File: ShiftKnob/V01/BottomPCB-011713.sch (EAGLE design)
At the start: 20 parts, among them Q1 16MHz, U1 ATMEGA328, U2 MIC5205-5.0BM5

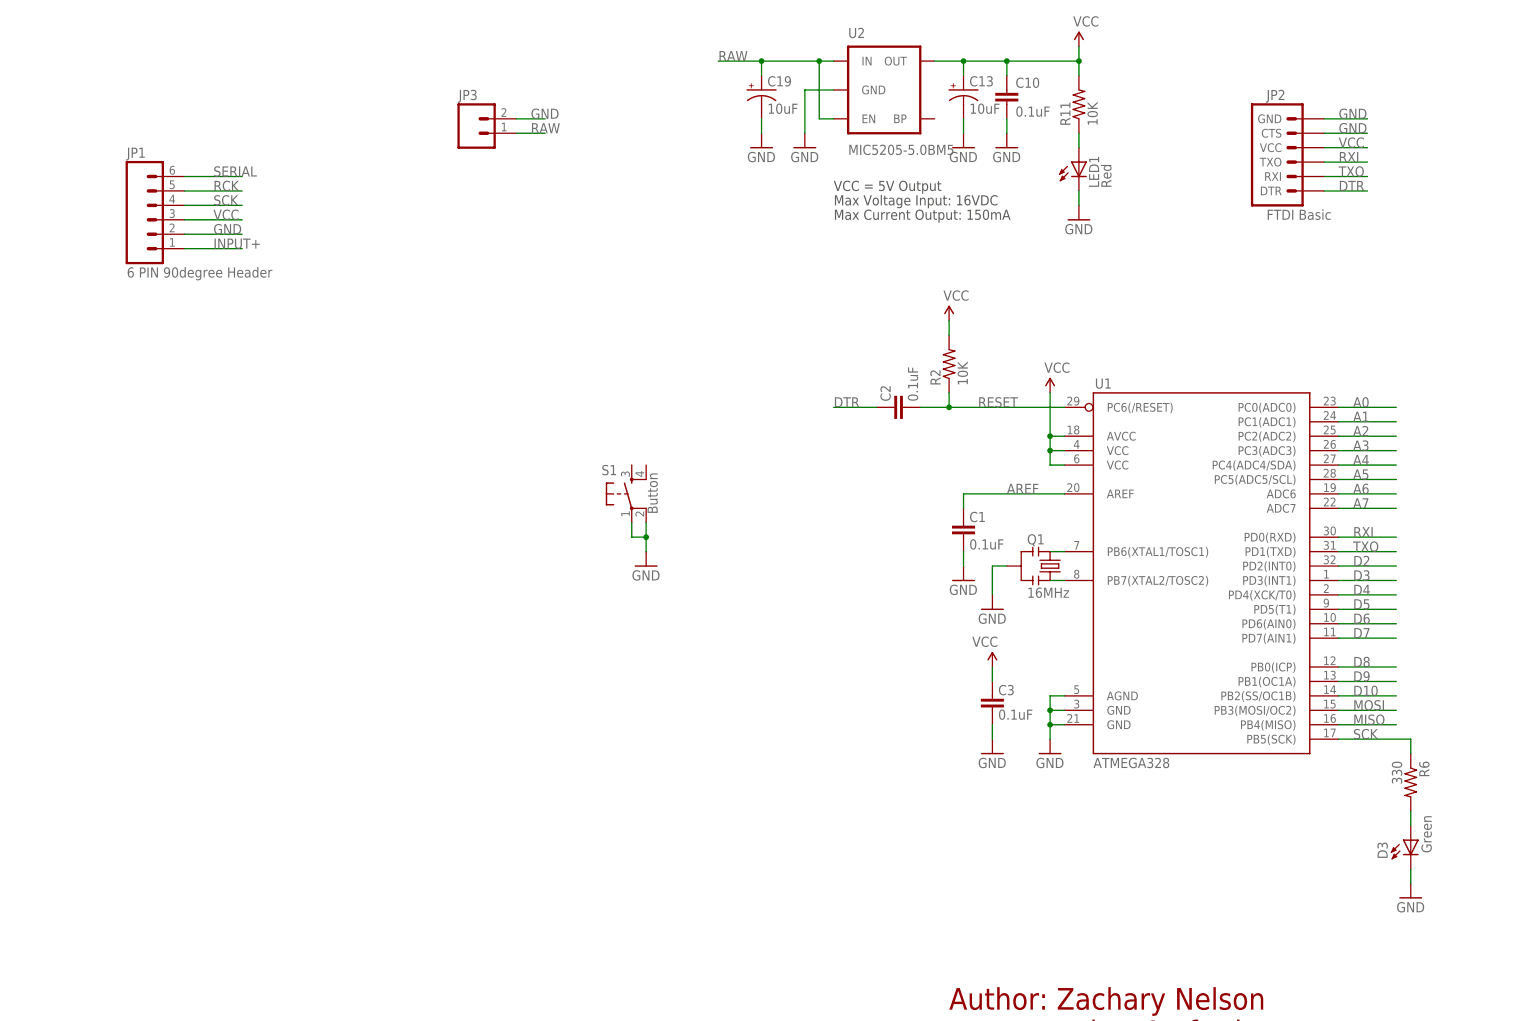
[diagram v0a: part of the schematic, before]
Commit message: all components added to BottomPCB schematic. added: MOSFETs, RGB LEDs x2, Motor connector, 7805 regulator
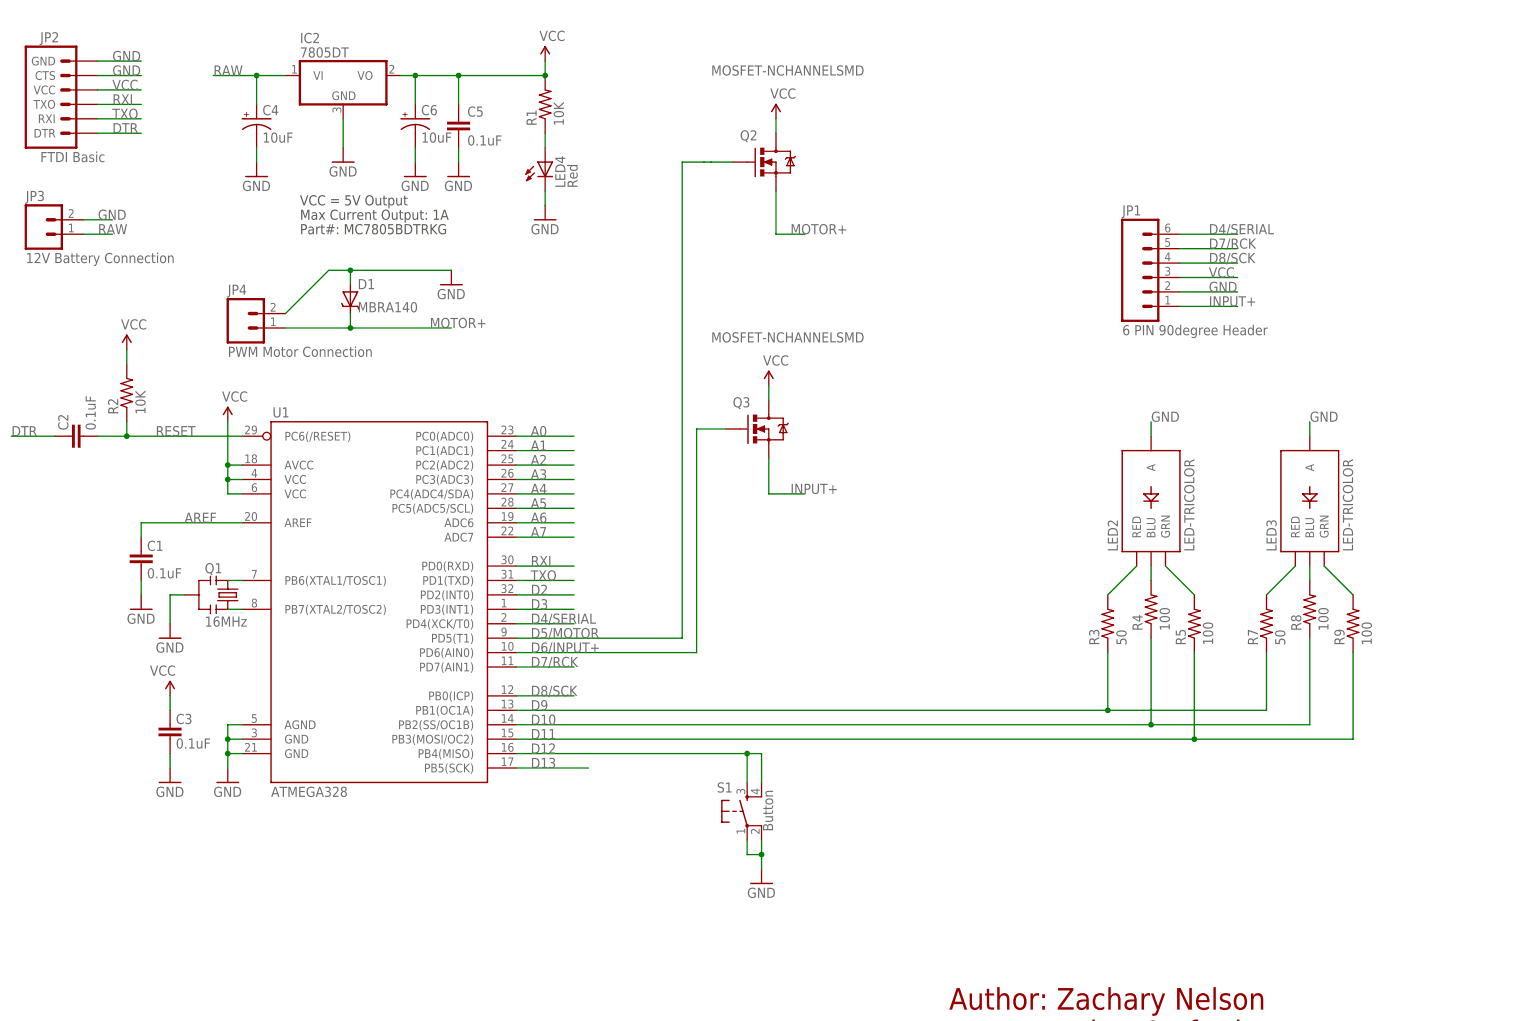
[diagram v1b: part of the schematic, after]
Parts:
- removed C10: 0.1uF, SparkFun:CAP0402-CAP
- removed C13, C19: 10uF, SparkFun:CAP_POL1206
- removed D3: Green, SparkFun:LED0603
- removed LED1: Red, SparkFun:LED0603
- removed R11: 10K, SparkFun:RESISTOR0402-RES
- removed R6: 330, SparkFun:RESISTOR0402-RES
- removed U2: MIC5205-5.0BM5, SparkFun:V_REG_LDOSMD
- added C4, C6: 10uF, SparkFun:CAP_POL1206
- added C5: 0.1uF, SparkFun:CAP0402-CAP
- added D1: MBRA140, SparkFun-DiscreteSemi:MBRA140
- added IC2: 7805DT, linear:7805DT
- added JP4: PWM Motor Connection, SparkFun-Connectors:M02POLAR
- added LED2, LED3: LED-TRICOLOR, SparkFun:LED-TRICOLOR
- added LED4: Red, SparkFun:LED0603
- added Q2, Q3: MOSFET-NCHANNELSMD, SparkFun-DiscreteSemi:MOSFET-NCHANNELSMD
- added R1: 10K, SparkFun:RESISTOR0402-RES
- added R3, R7: 50, SparkFun-Resistors:RESISTOR0805-RES
- added R4, R5, R8, R9: 100, SparkFun-Resistors:RESISTOR0805-RES
- JP3: value (none) -> 12V Battery Connection
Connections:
- removed net D4: U1.PD4(XCK/T0)
- removed net D5: U1.PD5(T1)
- removed net D6: U1.PD6(AIN0)
- removed net D7: U1.PD7(AIN1)
- removed net D8: U1.PB0(ICP)
- removed net MISO: U1.PB4(MISO)
- removed net MOSI: U1.PB3(MOSI/OC2)
- removed net N$38: LED1.A, R11.1
- removed net N$7: D3.A, R6.2
- removed net RCK: JP1.5
- removed net SCK: JP1.4, R6.1, U1.PB5(SCK)
- removed net SERIAL: JP1.6
- new net 3.3V: Q2.D, Q3.D
- new net D11: R5.1, R9.1, U1.PB3(MOSI/OC2)
- new net D12: S1.3, S1.4, U1.PB4(MISO)
- new net D13: U1.PB5(SCK)
- new net D4/SERIAL: JP1.6, U1.PD4(XCK/T0)
- new net D5/MOTOR: Q2.G, U1.PD5(T1)
- new net D6/INPUT+: Q3.G, U1.PD6(AIN0)
- new net D7/RCK: JP1.5, U1.PD7(AIN1)
- new net D8/SCK: JP1.4, U1.PB0(ICP)
- new net MOTOR+: D1.C, JP4.1, Q2.S
- new net N$16: LED3.BLU, R8.2
- new net N$25: LED2.BLU, R4.2
- new net N$3: LED4.A, R1.1
- new net N$4: LED2.RED, R3.2
- new net N$5: LED2.GRN, R5.2
- new net N$6: LED3.RED, R7.2
- new net N$8: LED3.GRN, R9.2
- net D10: now also R4.1, R8.1
- net D9: now also R3.1, R7.1
- net GND: now also C4.-, C5.2, C6.-, D1.A, IC2.GND, JP4.2, LED2.A, LED3.A, LED4.C; no longer C10.2, C13.-, C19.-, D3.C, LED1.C, U2.GND
- net INPUT+: now also Q3.S
- net RAW: now also C4.+, IC2.VI; no longer C19.+, U2.EN, U2.IN
- net VCC: now also C5.1, C6.+, IC2.VO, R1.2; no longer C10.1, C13.+, R11.2, U2.OUT
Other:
- note added: "Max Current Output: 1A"
- note added: "Part#: MC7805BDTRKG"
- note removed: "Max Current Output: 150mA"
- note removed: "Max Voltage Input: 16VDC"
- moved on the sheet: C1, C2, C3, JP1, JP2, JP3, Q1, R2, S1, U1

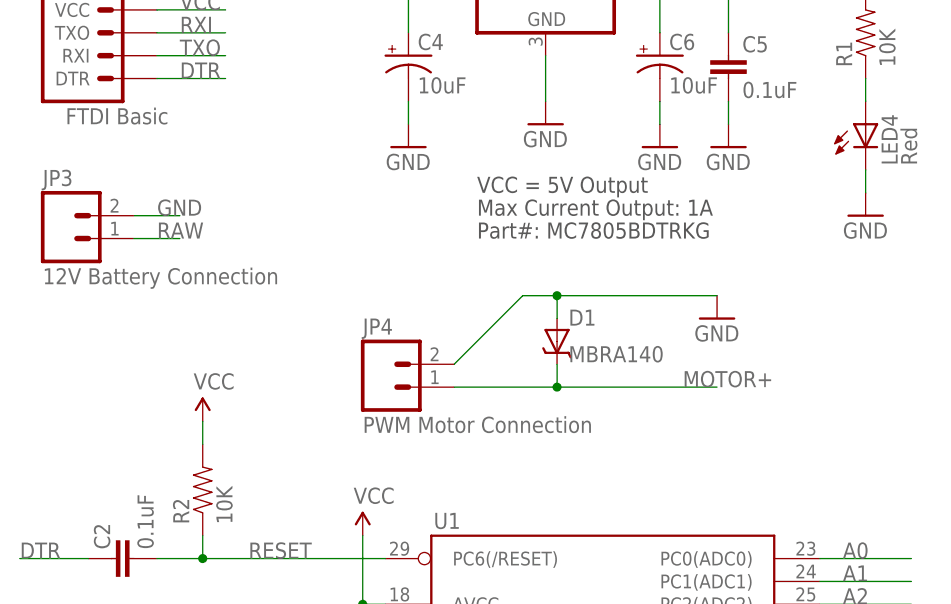
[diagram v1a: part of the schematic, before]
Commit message: change battery and motor connectors to SMT parts
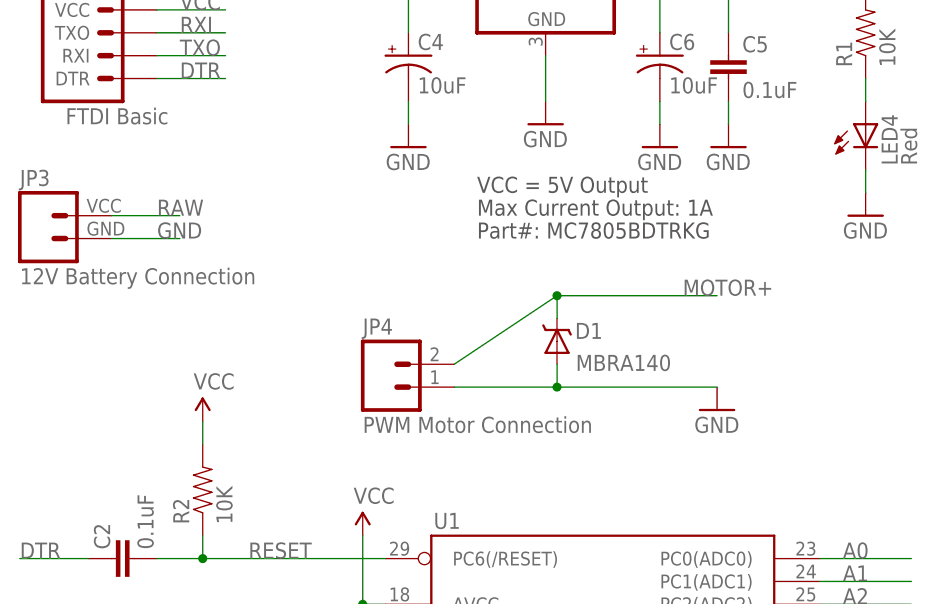
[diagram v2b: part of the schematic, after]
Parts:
- JP3: device SparkFun-Connectors:M02POLAR -> SparkFun-Connectors:M024UCON-15767
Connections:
- removed net 3.3V: Q2.D, Q3.D
- net GND: now also JP3.1, JP4.1; no longer JP3.2, JP4.2
- net MOTOR+: now also JP4.2; no longer JP4.1
- net RAW: now also JP3.2; no longer JP3.1
- net VCC: now also Q2.D, Q3.D
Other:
- moved on the sheet: D1, JP3

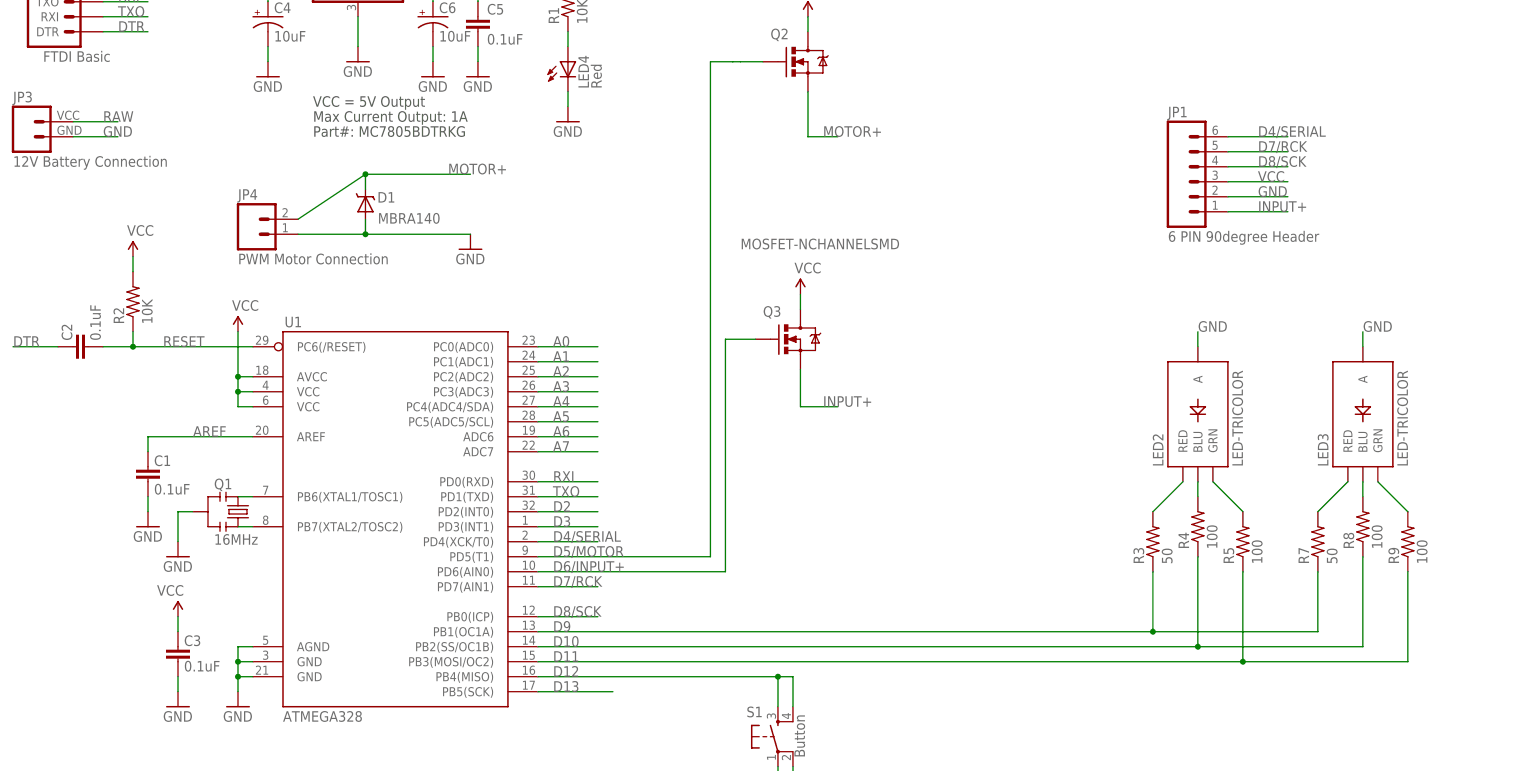
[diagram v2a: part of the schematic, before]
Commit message: add 1 more RGB led. add FETs for controlling 3 LEDs.
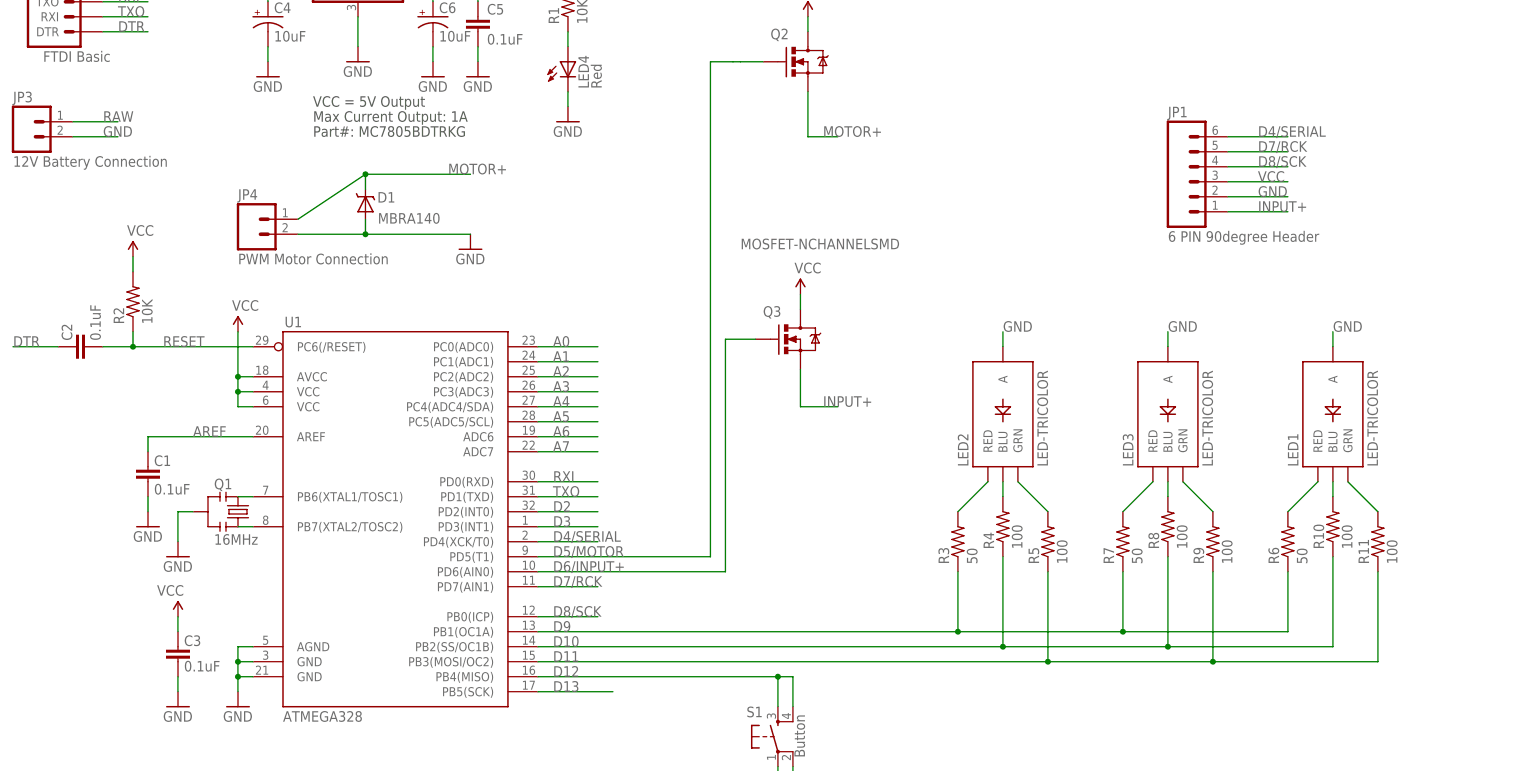
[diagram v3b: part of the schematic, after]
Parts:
- added LED1: LED-TRICOLOR, SparkFun:LED-TRICOLOR
- added R10, R11: 100, SparkFun-Resistors:RESISTOR0805-RES
- added R6: 50, SparkFun-Resistors:RESISTOR0805-RES
- JP3: device SparkFun-Connectors:M024UCON-15767 -> SparkFun-Connectors:M02-JST-2MM-SMT; PROD_ID (none) -> CONN-08352
- JP4: device SparkFun-Connectors:M02POLAR -> SparkFun-Connectors:M02-JST-2MM-SMT
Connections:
- new net N$10: LED1.GRN, R11.2
- new net N$7: LED1.BLU, R10.2
- new net N$9: LED1.RED, R6.2
- net D10: now also R10.1
- net D11: now also R11.1
- net D9: now also R6.1
- net GND: now also LED1.A
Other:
- moved on the sheet: JP3, LED2, LED3, R3, R4, R5, R7, R8, R9
